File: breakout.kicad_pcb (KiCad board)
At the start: 2 copper layers, 25.9 x 20.8 mm, 11 parts, among them P1 CONN_01X08, P2 CONN_01X08, U1 ESP-12E, U2 APE8865Y5-33-HF-3

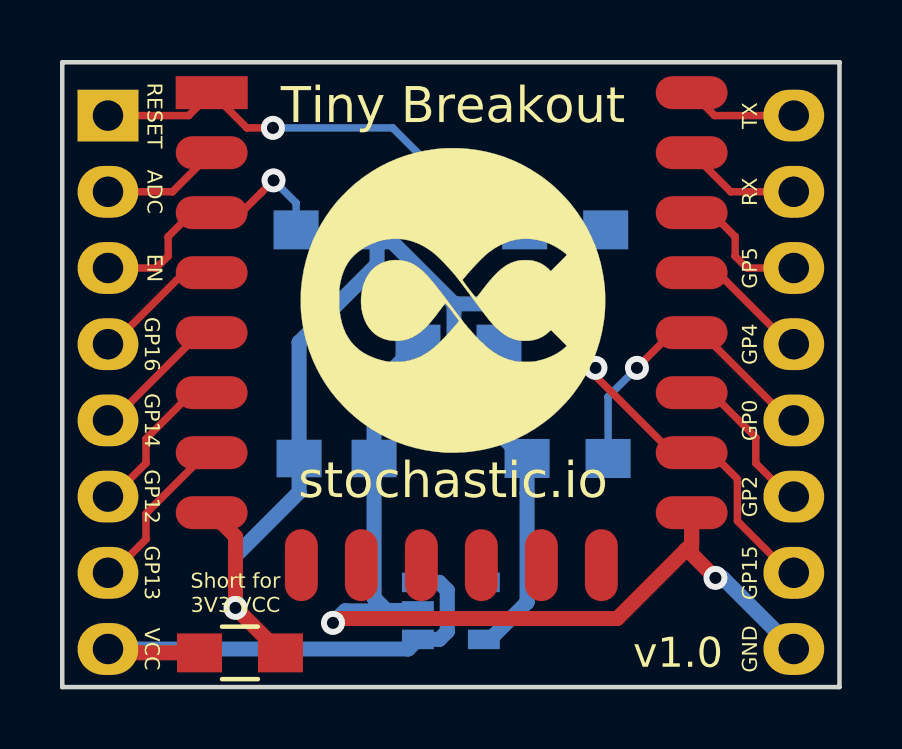
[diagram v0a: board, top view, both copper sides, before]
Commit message: Add pullup resistor to GPIO2.
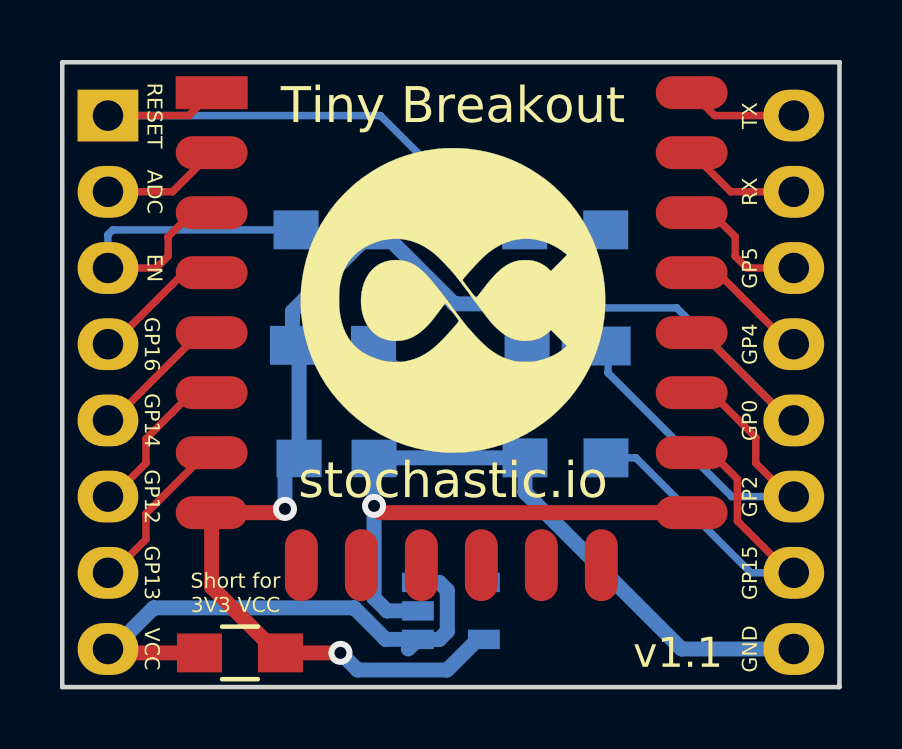
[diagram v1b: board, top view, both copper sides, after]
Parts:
- added R6: 10KΩ, Resistors_SMD:R_0805_HandSoldering, B.Cu at (134.5, 61.0)
- moved R3 5.20 mm to (142.2, 64.8)
- moved R4 3.75 mm to (142.3, 61.0)
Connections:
- R4 pad 2: Net-(P2-Pad5) -> Net-(P2-Pad6)
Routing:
- net Net-(P2-Pad5): track 10.5 -> 24.9 mm, vias 1 -> 0
- net Net-(P2-Pad6): track 5.34 -> 14.8 mm
- net /3V3: track 43.9 -> 39.1 mm, vias 1 -> 2
- net Net-(P1-Pad3): track 10.00 -> 14.0 mm, vias 1 -> 0
- net Net-(P1-Pad1): track 16.2 -> 19.3 mm, vias 1 -> 0
- net +12V: track 17.1 -> 18.4 mm
- net Net-(P2-Pad7): track 14.5 -> 15.6 mm, vias 1 -> 0
- net GND: track 34.2 -> 34.5 mm, vias 2 -> 1
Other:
- board text added: "R6"
- board text added: "v1.1"
- board text removed: "v1.0"

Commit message: Clean up, enlarge vias.
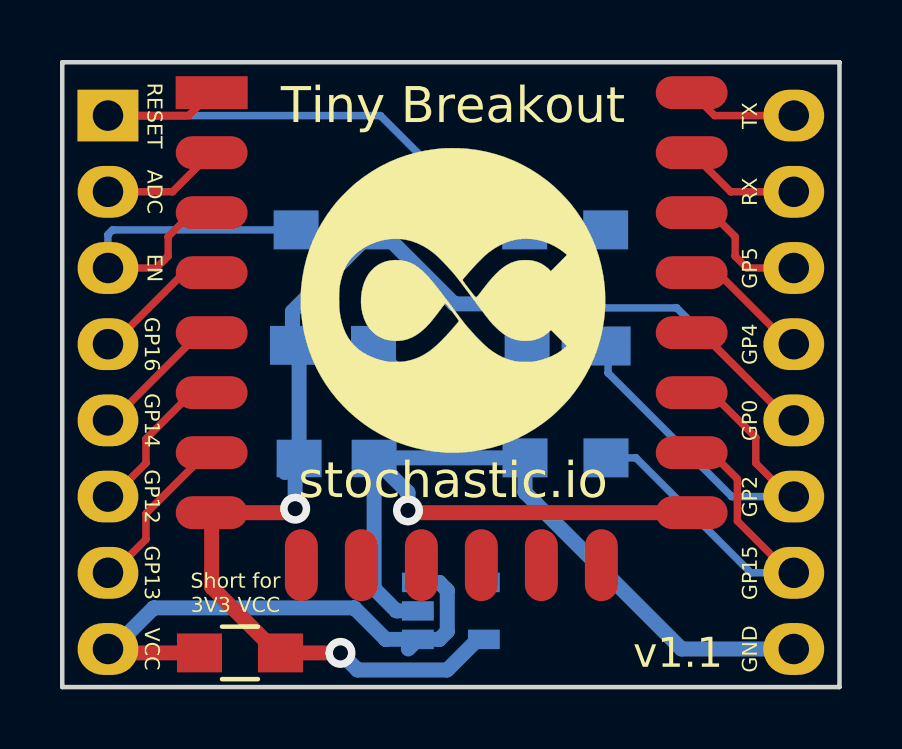
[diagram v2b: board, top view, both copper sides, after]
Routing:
- net /3V3: track 39.1 -> 40.0 mm
- net GND: track 34.5 -> 35.4 mm
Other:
- net class Power: via_dia 0.8 -> 1; via_drill 0.4 -> 0.5
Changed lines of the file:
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@@
     (links 33)
     (no_connects 0)
-    (area 125.400999 51.486999 151.459001 72.465001)
+    (area 121.891667 43.899799 154.968334 74.325)
     (thickness 1.6)
     (drawings 31)
-    (tracks 141)
+    (tracks 145)
     (zones 0)
     (modules 12)
@@
     (visible_elements FFFFFF7F)
     (pcbplotparams
-      (layerselection 0x00030_ffffffff)
-      (usegerberextensions false)
+      (layerselection 0x010f0_ffffffff)
+      (usegerberextensions true)
       (excludeedgelayer true)
       (linewidth 0.100000)
@@
       (outputformat 1)
       (mirror false)
-      (drillshape 1)
+      (drillshape 0)
       (scaleselection 1)
-      (outputdirectory ""))
+      (outputdirectory ../../gerbs/))
   )
   (net 0 "")
@@
     (clearance 0.2)
     (trace_width 0.5)
-    (via_dia 0.8)
-    (via_drill 0.4)
+    (via_dia 1)
+    (via_drill 0.5)
     (uvia_dia 0.3)
     (uvia_drill 0.1)
@@
   (segment (start 127.13 71.25) (end 127 71.12) (width 0.5) (layer F.Cu) (net 15) (status 30))
   (segment (start 137.01 71.12) (end 137.33 70.8) (width 0.5) (layer B.Cu) (net 15) (status 30))
-  (segment (start 135.87 66.35) (end 135.87 69.42) (width 0.5) (layer B.Cu) (net 16))
-  (segment (start 136.3 69.85) (end 137.33 69.85) (width 0.5) (layer B.Cu) (net 16) (status 20))
-  (segment (start 135.87 69.42) (end 136.3 69.85) (width 0.5) (layer B.Cu) (net 16))
+  (segment (start 137 66.5) (end 137 65.9) (width 0.5) (layer B.Cu) (net 16))
+  (segment (start 137 65.9) (end 135.87 64.77) (width 0.5) (layer B.Cu) (net 16))
+  (segment (start 146.456 66.576) (end 137.076 66.576) (width 0.5) (layer F.Cu) (net 16))
+  (segment (start 137.076 66.576) (end 137 66.5) (width 0.5) (layer F.Cu) (net 16))
+  (via (at 137 66.5) (size 1) (drill 0.5) (layers F.Cu B.Cu) (net 16))
+  (segment (start 146.12 71.12) (end 141.25 66.25) (width 0.5) (layer B.Cu) (net 16))
+  (segment (start 141.25 66.25) (end 140.9 65.9) (width 0.5) (layer B.Cu) (net 16))
+  (segment (start 137.33 69.85) (end 136.614998 69.85) (width 0.5) (layer B.Cu) (net 16))
+  (segment (start 136.614998 69.85) (end 135.87 69.105002) (width 0.5) (layer B.Cu) (net 16))
+  (segment (start 135.87 69.105002) (end 135.87 65.895) (width 0.5) (layer B.Cu) (net 16))
+  (segment (start 135.87 65.895) (end 135.87 64.77) (width 0.5) (layer B.Cu) (net 16))
   (segment (start 149.86 71.12) (end 146.12 71.12) (width 0.5) (layer B.Cu) (net 16))
   (segment (start 140.9 65.9) (end 140.9 64.75) (width 0.5) (layer B.Cu) (net 16))
-  (segment (start 146.12 71.12) (end 140.9 65.9) (width 0.5) (layer B.Cu) (net 16))
   (segment (start 140.9 64.75) (end 135.89 64.75) (width 0.5) (layer B.Cu) (net 16) (status 30))
   (segment (start 135.89 64.75) (end 135.87 64.77) (width 0.5) (layer B.Cu) (net 16) (status 30))
-  (segment (start 135.87 64.77) (end 135.87 66.35) (width 0.5) (layer B.Cu) (net 16) (status 10))
-  (segment (start 146.456 66.576) (end 136.096 66.576) (width 0.5) (layer F.Cu) (net 16) (status 10))
-  (segment (start 136.096 66.576) (end 135.87 66.35) (width 0.5) (layer F.Cu) (net 16))
-  (via (at 135.87 66.35) (size 0.8) (drill 0.4) (layers F.Cu B.Cu) (net 16))
   (segment (start 149.86 71.12) (end 149.7076 71.12) (width 0.5) (layer B.Cu) (net 16) (status 30))
   (segment (start 140.97 64.77) (end 140.87 64.77) (width 0.5) (layer B.Cu) (net 16) (status 30))
-  (segment (start 134.75 71.25) (end 132.75 71.25) (width 0.5) (layer F.Cu) (net 17))
+  (segment (start 133.2405 66.442998) (end 133.2405 64.8995) (width 0.5) (layer B.Cu) (net 17))
+  (segment (start 133.2405 64.8995) (end 133.37 64.77) (width 0.5) (layer B.Cu) (net 17))
+  (segment (start 130.456 66.576) (end 133.107498 66.576) (width 0.5) (layer F.Cu) (net 17))
+  (segment (start 133.107498 66.576) (end 133.2405 66.442998) (width 0.5) (layer F.Cu) (net 17))
+  (via (at 133.2405 66.442998) (size 1) (drill 0.5) (layers F.Cu B.Cu) (net 17))
+  (via (at 134.75 71.25) (size 1) (drill 0.5) (layers F.Cu B.Cu) (net 17))
+  (segment (start 132.75 71.25) (end 134.75 71.25) (width 0.5) (layer F.Cu) (net 17))
   (segment (start 139.53 70.8) (end 139.325 70.8) (width 0.5) (layer B.Cu) (net 17))
   (segment (start 138.304992 71.820008) (end 135.320008 71.820008) (width 0.5) (layer B.Cu) (net 17))
   (segment (start 139.325 70.8) (end 138.304992 71.820008) (width 0.5) (layer B.Cu) (net 17))
   (segment (start 135.320008 71.820008) (end 134.75 71.25) (width 0.5) (layer B.Cu) (net 17))
-  (via (at 134.75 71.25) (size 0.8) (drill 0.4) (layers F.Cu B.Cu) (net 17))
   (segment (start 141.025999 59.614001) (end 140.5 59.614001) (width 0.5) (layer B.Cu) (net 17))
   (segment (start 140.5 59.614001) (end 138.534001 59.614001) (width 0.5) (layer B.Cu) (net 17))
@@
   (segment (start 135.87 57.15) (end 133.15 59.87) (width 0.5) (layer B.Cu) (net 17) (status 10))
   (segment (start 133.15 59.87) (end 133.15 61) (width 0.5) (layer B.Cu) (net 17) (status 20))
-  (segment (start 132.9 66.45) (end 132.9 65.24) (width 0.5) (layer B.Cu) (net 17) (status 20))
   (segment (start 132.9 65.24) (end 133.37 64.77) (width 0.5) (layer B.Cu) (net 17) (status 30))
-  (segment (start 130.456 66.576) (end 132.774 66.576) (width 0.5) (layer F.Cu) (net 17) (status 10))
-  (segment (start 132.774 66.576) (end 132.9 66.45) (width 0.5) (layer F.Cu) (net 17))
-  (via (at 132.9 66.45) (size 0.8) (drill 0.4) (layers F.Cu B.Cu) (net 17))
   (segment (start 130.456 66.576) (end 130.456 69.056) (width 0.5) (layer F.Cu) (net 17) (status 10))
   (segment (start 130.456 69.056) (end 132.65 71.25) (width 0.5) (layer F.Cu) (net 17) (status 20))

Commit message: Increase power via size.
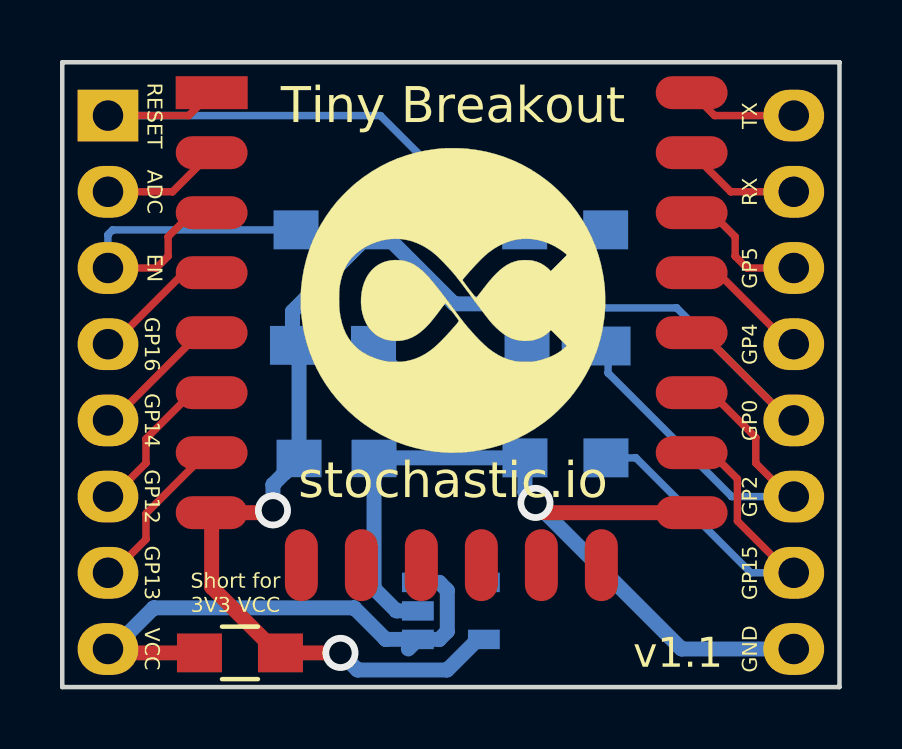
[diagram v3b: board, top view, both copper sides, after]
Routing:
- net GND: track 35.4 -> 29.0 mm
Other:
- net class Power: via_dia 1 -> 1.2; via_drill 0.5 -> 0.75
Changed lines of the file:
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@@
     (links 33)
     (no_connects 0)
-    (area 121.891667 43.899799 154.968334 74.325)
+    (area 125.400999 51.486999 151.459001 72.465001)
     (thickness 1.6)
     (drawings 31)
-    (tracks 145)
+    (tracks 144)
     (zones 0)
     (modules 12)
@@
     (clearance 0.2)
     (trace_width 0.5)
-    (via_dia 1)
-    (via_drill 0.5)
+    (via_dia 1.2)
+    (via_drill 0.75)
     (uvia_dia 0.3)
     (uvia_drill 0.1)
@@
       (effects (font (size 1 1) (thickness 0.15)))
     )
-    (fp_text value 0Ω (at 0 2.1) (layer F.Fab)
+    (fp_text value 0Ω (at 0 2.1) (layer F.Fab) hide
       (effects (font (size 1 1) (thickness 0.15)))
     )
@@
   (segment (start 127.13 71.25) (end 127 71.12) (width 0.5) (layer F.Cu) (net 15) (status 30))
   (segment (start 137.01 71.12) (end 137.33 70.8) (width 0.5) (layer B.Cu) (net 15) (status 30))
-  (segment (start 137 66.5) (end 137 65.9) (width 0.5) (layer B.Cu) (net 16))
-  (segment (start 137 65.9) (end 135.87 64.77) (width 0.5) (layer B.Cu) (net 16))
-  (segment (start 146.456 66.576) (end 137.076 66.576) (width 0.5) (layer F.Cu) (net 16))
-  (segment (start 137.076 66.576) (end 137 66.5) (width 0.5) (layer F.Cu) (net 16))
-  (via (at 137 66.5) (size 1) (drill 0.5) (layers F.Cu B.Cu) (net 16))
+  (segment (start 146.456 66.576) (end 141.576 66.576) (width 0.5) (layer F.Cu) (net 16))
+  (segment (start 141.576 66.576) (end 141.25 66.25) (width 0.5) (layer F.Cu) (net 16))
+  (via (at 141.25 66.25) (size 1.2) (drill 0.75) (layers F.Cu B.Cu) (net 16))
   (segment (start 146.12 71.12) (end 141.25 66.25) (width 0.5) (layer B.Cu) (net 16))
   (segment (start 141.25 66.25) (end 140.9 65.9) (width 0.5) (layer B.Cu) (net 16))
@@
   (segment (start 149.86 71.12) (end 149.7076 71.12) (width 0.5) (layer B.Cu) (net 16) (status 30))
   (segment (start 140.97 64.77) (end 140.87 64.77) (width 0.5) (layer B.Cu) (net 16) (status 30))
-  (segment (start 133.2405 66.442998) (end 133.2405 64.8995) (width 0.5) (layer B.Cu) (net 17))
+  (segment (start 132.5 66.5) (end 132.5 65.64) (width 0.5) (layer B.Cu) (net 17))
+  (segment (start 132.5 65.64) (end 133.37 64.77) (width 0.5) (layer B.Cu) (net 17))
+  (segment (start 130.456 66.576) (end 132.424 66.576) (width 0.5) (layer F.Cu) (net 17))
+  (segment (start 132.424 66.576) (end 132.5 66.5) (width 0.5) (layer F.Cu) (net 17))
+  (via (at 132.5 66.5) (size 1.2) (drill 0.75) (layers F.Cu B.Cu) (net 17))
   (segment (start 133.2405 64.8995) (end 133.37 64.77) (width 0.5) (layer B.Cu) (net 17))
-  (segment (start 130.456 66.576) (end 133.107498 66.576) (width 0.5) (layer F.Cu) (net 17))
-  (segment (start 133.107498 66.576) (end 133.2405 66.442998) (width 0.5) (layer F.Cu) (net 17))
-  (via (at 133.2405 66.442998) (size 1) (drill 0.5) (layers F.Cu B.Cu) (net 17))
-  (via (at 134.75 71.25) (size 1) (drill 0.5) (layers F.Cu B.Cu) (net 17))
+  (via (at 134.75 71.25) (size 1.2) (drill 0.75) (layers F.Cu B.Cu) (net 17))
   (segment (start 132.75 71.25) (end 134.75 71.25) (width 0.5) (layer F.Cu) (net 17))
   (segment (start 139.53 70.8) (end 139.325 70.8) (width 0.5) (layer B.Cu) (net 17))
